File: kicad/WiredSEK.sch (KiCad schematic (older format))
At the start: 51 parts, among them J1 Conn_01x34, J2 USB_C_Receptacle, J3 AVR-JTAG-10, J4 Serial RX/TX, J5 Testpad, SW1 HWB_SW, SW2 RST_SW, U1 USBLC6-2SC6, U2 AT90USB646-AU, Y1 16 Mhz

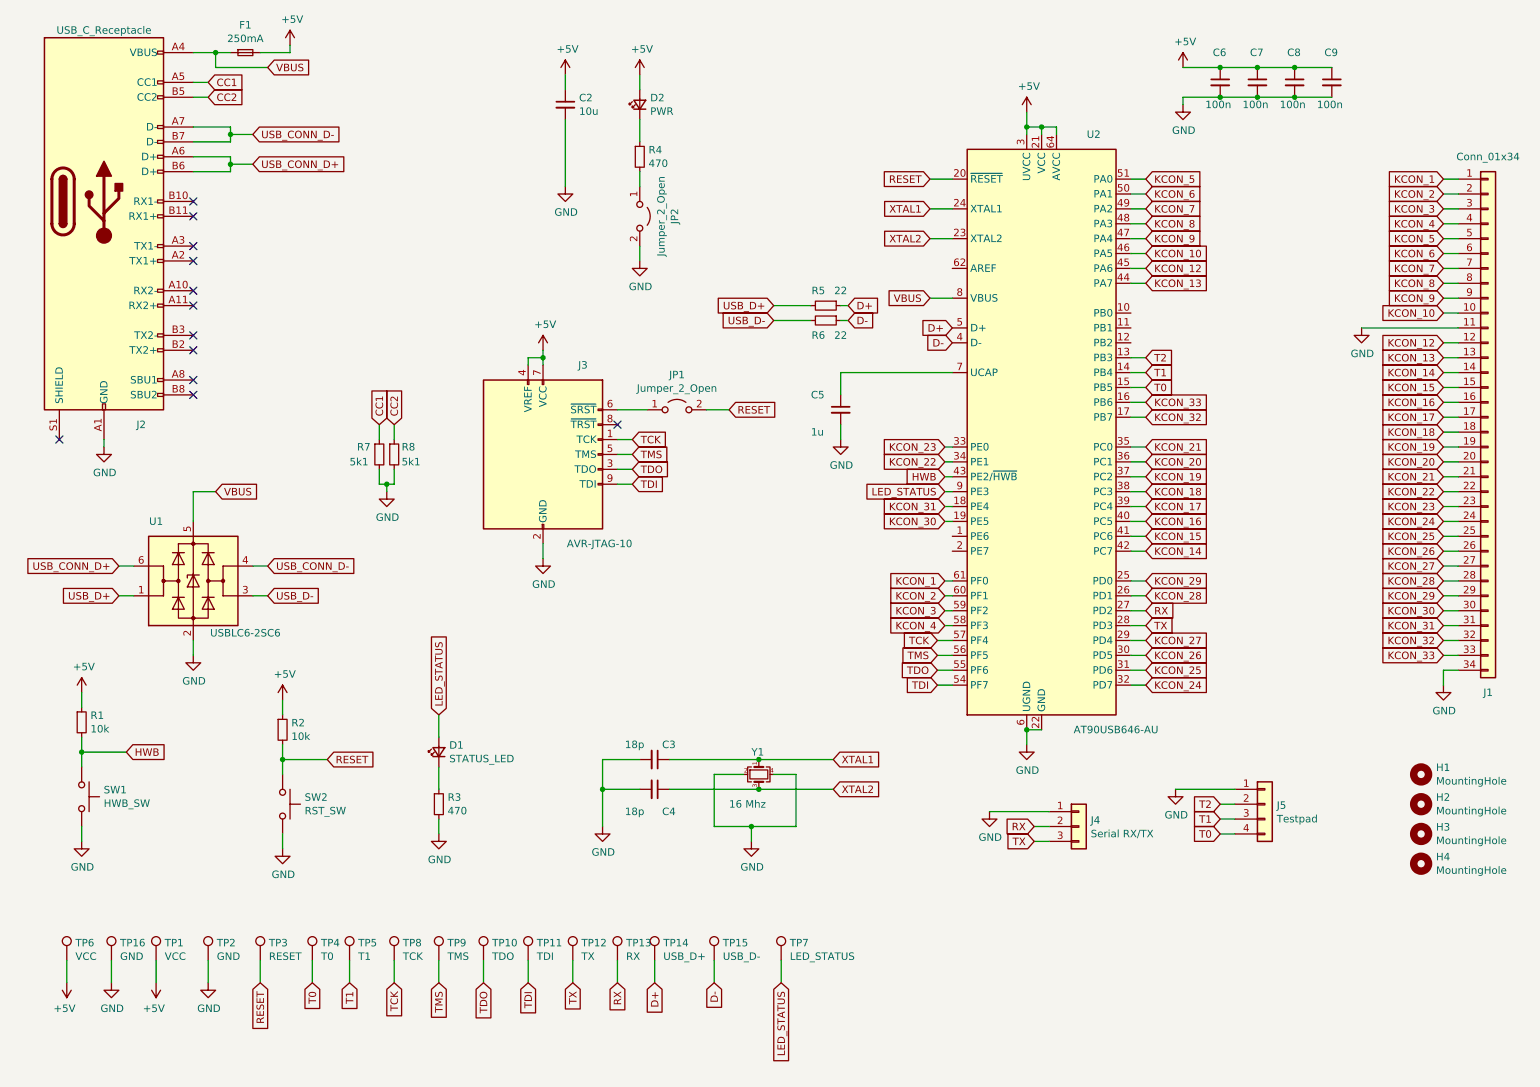
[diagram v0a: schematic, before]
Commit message: done with pcb routing
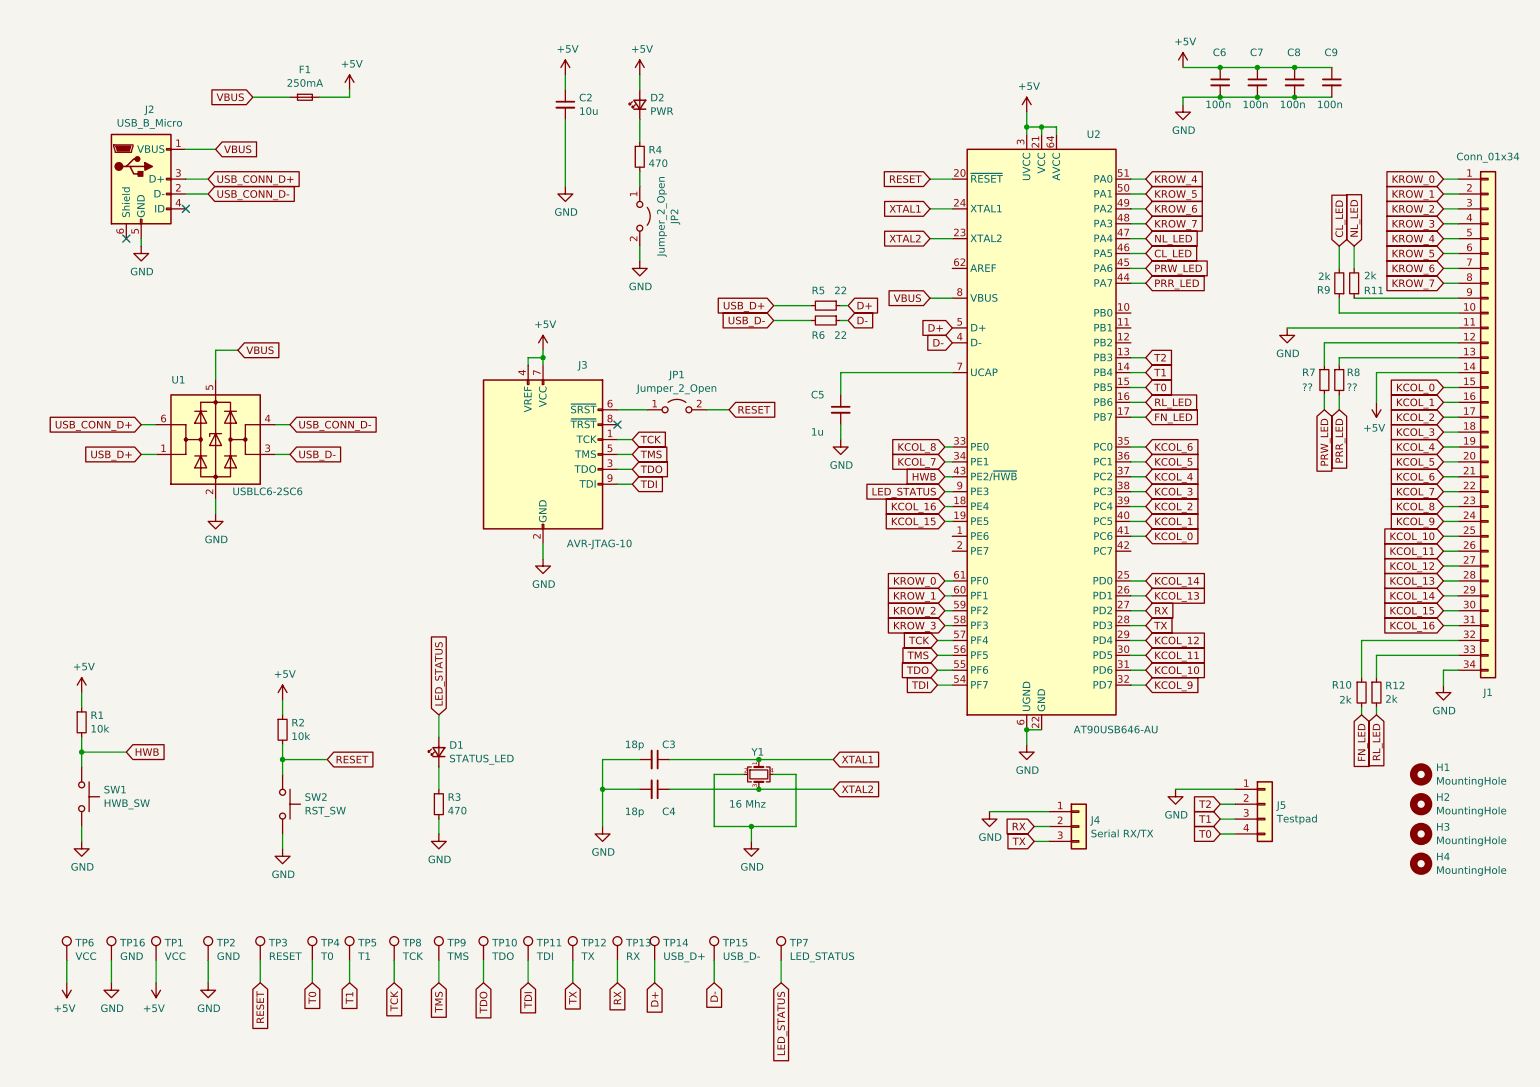
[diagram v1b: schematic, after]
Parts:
- removed J2: USB_C_Receptacle, WiredSEK:SJ121226, symbol Connector:USB_C_Receptacle
- added J2: USB_B_Micro, WiredSEK:GMCB05801124EU, symbol Connector:USB_B_Micro
- added R10, R11, R12, R9: 2k, Resistor_SMD:R_0805_2012Metric_Pad1.20x1.40mm_HandSolder, symbol Device:R_Small
- R7, R8: value 5k1 -> ??; JLCPCB C27834 -> C17710
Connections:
- net +5V: now also J1.14 (Pin_14)
- net GND: now also J2.5 (GND); no longer R7.2, R8.2
- net USB_CONN_D+: now also J2.3 (D+)
- net USB_CONN_D-: now also J2.2 (D-)
- net VBUS: now also J2.1 (VBUS)
- net CC1: no longer names the net of R7.1
- net CC1: now also J1.12 (Pin_12)
- net CC2: no longer names the net of R8.1
- net CC2: now also J1.13 (Pin_13)
- net KCON_1 renamed KROW_0
- net KCON_10: no longer names the net of J1.10 (Pin_10)
- net KCON_10: now also R9.1; no longer U2.46 (PA5)
- net KCON_12 renamed PRW_LED
- net PRW_LED: now also R7.2; no longer J1.12 (Pin_12)
- net KCON_13 renamed PRR_LED
- net PRR_LED: now also R8.2; no longer J1.13 (Pin_13)
- net KCON_14: no longer names the net of U2.42 (PC7)
- net KCON_14: no longer J1.14 (Pin_14)
- net KCON_15 renamed KCOL_0
- net KCON_16 renamed KCOL_1
- net KCON_17 renamed KCOL_2
- net KCON_18 renamed KCOL_3
- net KCON_19 renamed KCOL_4
- net KCON_2 renamed KROW_1
- net KCON_20 renamed KCOL_5
- net KCON_21 renamed KCOL_6
- net KCON_22 renamed KCOL_7
- net KCON_23 renamed KCOL_8
- net KCON_24 renamed KCOL_9
- net KCON_25 renamed KCOL_10
- net KCON_26 renamed KCOL_11
- net KCON_27 renamed KCOL_12
- net KCON_28 renamed KCOL_13
- net KCON_29 renamed KCOL_14
- net KCON_3 renamed KROW_2
- net KCON_30 renamed KCOL_15
- net KCON_31 renamed KCOL_16
- net KCON_32: no longer names the net of J1.32 (Pin_32)
- net KCON_32: now also R10.1; no longer U2.17 (PB7)
- net KCON_33: no longer names the net of J1.33 (Pin_33)
- net KCON_33: now also R12.1; no longer U2.16 (PB6)
- net KCON_4 renamed KROW_3
- net KCON_5 renamed KROW_4
- net KCON_6 renamed KROW_5
- net KCON_7 renamed KROW_6
- net KCON_8 renamed KROW_7
- net KCON_9: no longer names the net of J1.9 (Pin_9)
- net KCON_9: now also R11.1; no longer U2.47 (PA4)
- new net CL_LED: R9.2, U2.46 (PA5)
- new net FN_LED: R10.2, U2.17 (PB7)
- new net NL_LED: R11.2, U2.47 (PA4)
- new net RL_LED: R12.2, U2.16 (PB6)
- no-connect marks 12 -> 3
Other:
- moved on the sheet: F1, U1

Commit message: preparing for jlcpcb order
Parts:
- C2: JLCPCB C15850 -> (none); LCSC Part # (none) -> C15850
- C3, C4: JLCPCB C1647 -> (none); LCSC Part # (none) -> C1647
- C5: LCSC Part # (none) -> C15849
- C6, C7, C8, C9: JLCPCB C57112 -> (none); LCSC Part # (none) -> C57112
- D1: JLCPCB C72041 -> (none); LCSC Part # (none) -> C72041
- D2: JLCPCB C72043 -> (none); LCSC Part # (none) -> C72043
- F1: JLCPCB C369159 -> (none); LCSC Part # (none) -> C369159
- R1, R2: JLCPCB C17414 -> (none); LCSC Part # (none) -> C17414
- R10, R11, R12, R3, R4, R9: JLCPCB C17710 -> (none); LCSC Part # (none) -> C17710
- R5, R6: JLCPCB C25295 -> (none); LCSC Part # (none) -> C25295
- R7, R8: JLCPCB C17710 -> (none)
- SW1, SW2: JLCPCB C115357 -> (none); LCSC Part # (none) -> C115357
- U1: JLCPCB C558442 -> (none); LCSC Part # (none) -> C558442
- Y1: JLCPCB X1E000021011900 -> (none); LCSC Part # (none) -> X1E000021011900
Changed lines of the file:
@@
 F 2 "Package_TO_SOT_SMD:SOT-23-6" H 1900 2850 50  0001 C CNN
 F 3 "https://www.st.com/resource/en/datasheet/usblc6-2.pdf" H 2100 3700 50  0001 C CNN
-F 4 "C558442" H 1900 3350 50  0001 C CNN "JLCPCB"
+F 4 "C558442" H 1900 3350 50  0001 C CNN "LCSC Part #"
 	1    1900 3350
 	1    0    0    -1
@@
 F 2 "Resistor_SMD:R_0805_2012Metric_Pad1.20x1.40mm_HandSolder" H 6000 2450 50  0001 C CNN
 F 3 "~" H 6000 2450 50  0001 C CNN
-F 4 "C25295" V 6000 2450 50  0001 C CNN "JLCPCB"
+F 4 "C25295" H 6000 2450 50  0001 C CNN "LCSC Part #"
 	1    6000 2450
 	0    1    1    0
@@
 F 2 "Resistor_SMD:R_0805_2012Metric_Pad1.20x1.40mm_HandSolder" H 6000 2550 50  0001 C CNN
 F 3 "~" H 6000 2550 50  0001 C CNN
-F 4 "C25295" V 6000 2550 50  0001 C CNN "JLCPCB"
+F 4 "C25295" H 6000 2550 50  0001 C CNN "LCSC Part #"
 	1    6000 2550
 	0    1    1    0
@@
 F 2 "Capacitor_SMD:C_0603_1608Metric_Pad1.08x0.95mm_HandSolder" H 8650 950 50  0001 C CNN
 F 3 "~" H 8650 950 50  0001 C CNN
-F 4 "C57112" H 8650 950 50  0001 C CNN "JLCPCB"
+F 4 "C57112" H 8650 950 50  0001 C CNN "LCSC Part #"
 	1    8650 950
 	1    0    0    -1
@@
 F 2 "Capacitor_SMD:C_0603_1608Metric_Pad1.08x0.95mm_HandSolder" H 8900 950 50  0001 C CNN
 F 3 "~" H 8900 950 50  0001 C CNN
-F 4 "C57112" H 8900 950 50  0001 C CNN "JLCPCB"
+F 4 "C57112" H 8900 950 50  0001 C CNN "LCSC Part #"
 	1    8900 950
 	1    0    0    -1
@@
 F 2 "Capacitor_SMD:C_0603_1608Metric_Pad1.08x0.95mm_HandSolder" H 9150 950 50  0001 C CNN
 F 3 "~" H 9150 950 50  0001 C CNN
-F 4 "C57112" H 9150 950 50  0001 C CNN "JLCPCB"
+F 4 "C57112" H 9150 950 50  0001 C CNN "LCSC Part #"
 	1    9150 950
 	1    0    0    -1
@@
 F 2 "Capacitor_SMD:C_0603_1608Metric_Pad1.08x0.95mm_HandSolder" H 6100 3150 50  0001 C CNN
 F 3 "~" H 6100 3150 50  0001 C CNN
+F 4 "C15849" H 6100 3150 50  0001 C CNN "LCSC Part #"
 	1    6100 3150
 	1    0    0    -1
@@
 F 2 "Capacitor_SMD:C_0805_2012Metric_Pad1.18x1.45mm_HandSolder" H 4250 1100 50  0001 C CNN
 F 3 "~" H 4250 1100 50  0001 C CNN
-F 4 "C15850" H 4250 1100 50  0001 C CNN "JLCPCB"
+F 4 "C15850" H 4250 1100 50  0001 C CNN "LCSC Part #"
 	1    4250 1100
 	1    0    0    -1
@@
 	1    0    0    -1
 $EndComp
-Wire Wire Line
-	4250 1000 4250 900
 $Comp
 L Device:Crystal_GND24_Small Y1
@@
 F 2 "Crystal:Crystal_SMD_3225-4Pin_3.2x2.5mm_HandSoldering" H 5550 5600 50  0001 C CNN
 F 3 "~" H 5550 5600 50  0001 C CNN
-F 4 "X1E000021011900" V 5550 5600 50  0001 C CNN "JLCPCB"
+F 4 "X1E000021011900" H 5550 5600 50  0001 C CNN "LCSC Part #"
 	1    5550 5600
 	0    1    1    0
@@
 F 2 "Capacitor_SMD:C_0603_1608Metric_Pad1.08x0.95mm_HandSolder" H 4850 5500 50  0001 C CNN
 F 3 "~" H 4850 5500 50  0001 C CNN
-F 4 "C1647" V 4850 5500 50  0001 C CNN "JLCPCB"
+F 4 "C1647" H 4850 5500 50  0001 C CNN "LCSC Part #"
 	1    4850 5500
 	0    1    1    0
@@
 F 2 "Capacitor_SMD:C_0603_1608Metric_Pad1.08x0.95mm_HandSolder" H 4850 5700 50  0001 C CNN
 F 3 "~" H 4850 5700 50  0001 C CNN
-F 4 "C1647" V 4850 5700 50  0001 C CNN "JLCPCB"
+F 4 "C1647" H 4850 5700 50  0001 C CNN "LCSC Part #"
 	1    4850 5700
 	0    1    1    0
@@
 F 2 "Resistor_SMD:R_0805_2012Metric_Pad1.20x1.40mm_HandSolder" H 2350 5300 50  0001 C CNN
 F 3 "~" H 2350 5300 50  0001 C CNN
-F 4 "C17414" H 2350 5300 50  0001 C CNN "JLCPCB"
+F 4 "C17414" H 2350 5300 50  0001 C CNN "LCSC Part #"
 	1    2350 5300
 	1    0    0    -1
@@
 F 2 "WiredSEK:SKRKAEE020" H 2350 6000 50  0001 C CNN
 F 3 "~" H 2350 6000 50  0001 C CNN
-F 4 "C115357" V 2350 5800 50  0001 C CNN "JLCPCB"
+F 4 "C115357" H 2350 5800 50  0001 C CNN "LCSC Part #"
 	1    2350 5800
 	0    1    1    0
@@
 F 2 "Fuse:Fuse_1206_3216Metric_Pad1.42x1.75mm_HandSolder" H 2500 1050 50  0001 C CNN
 F 3 "~" H 2500 1050 50  0001 C CNN
-F 4 "C369159" H 2500 1050 50  0001 C CNN "JLCPCB"
+F 4 "C369159" H 2500 1050 50  0001 C CNN "LCSC Part #"
 	1    2500 1050
 	1    0    0    -1
@@
 F 2 "Resistor_SMD:R_0805_2012Metric_Pad1.20x1.40mm_HandSolder" H 1000 5250 50  0001 C CNN
 F 3 "~" H 1000 5250 50  0001 C CNN
-F 4 "C17414" H 1000 5250 50  0001 C CNN "JLCPCB"
+F 4 "C17414" H 1000 5250 50  0001 C CNN "LCSC Part #"
 	1    1000 5250
 	1    0    0    -1
@@
 F 2 "WiredSEK:SKRKAEE020" H 1000 5950 50  0001 C CNN
 F 3 "~" H 1000 5950 50  0001 C CNN
-F 4 "C115357" V 1000 5750 50  0001 C CNN "JLCPCB"
+F 4 "C115357" H 1000 5750 50  0001 C CNN "LCSC Part #"
 	1    1000 5750
 	0    1    1    0
@@
 F 2 "LED_SMD:LED_0603_1608Metric_Pad1.05x0.95mm_HandSolder" V 3400 5450 50  0001 C CNN
 F 3 "~" V 3400 5450 50  0001 C CNN
-F 4 "C72041" V 3400 5450 50  0001 C CNN "JLCPCB"
+F 4 "C72041" H 3400 5450 50  0001 C CNN "LCSC Part #"
 	1    3400 5450
 	0    -1   -1   0
@@
 F 2 "Resistor_SMD:R_0805_2012Metric_Pad1.20x1.40mm_HandSolder" H 3400 5800 50  0001 C CNN
 F 3 "~" H 3400 5800 50  0001 C CNN
-F 4 "C17710" H 3400 5800 50  0001 C CNN "JLCPCB"
+F 4 "C17710" H 3400 5800 50  0001 C CNN "LCSC Part #"
 	1    3400 5800
 	1    0    0    -1
@@
 F 2 "LED_SMD:LED_0603_1608Metric_Pad1.05x0.95mm_HandSolder" V 4750 1100 50  0001 C CNN
 F 3 "~" V 4750 1100 50  0001 C CNN
-F 4 "C72043" V 4750 1100 50  0001 C CNN "JLCPCB"
+F 4 "C72043" H 4750 1100 50  0001 C CNN "LCSC Part #"
 	1    4750 1100
 	0    -1   -1   0
@@
 F 2 "Resistor_SMD:R_0805_2012Metric_Pad1.20x1.40mm_HandSolder" H 4750 1450 50  0001 C CNN
 F 3 "~" H 4750 1450 50  0001 C CNN
-F 4 "C17710" H 4750 1450 50  0001 C CNN "JLCPCB"
+F 4 "C17710" H 4750 1450 50  0001 C CNN "LCSC Part #"
 	1    4750 1450
 	1    0    0    -1
@@
 F 2 "Capacitor_SMD:C_0603_1608Metric_Pad1.08x0.95mm_HandSolder" H 9400 950 50  0001 C CNN
 F 3 "~" H 9400 950 50  0001 C CNN
-F 4 "C57112" H 9400 950 50  0001 C CNN "JLCPCB"
+F 4 "C57112" H 9400 950 50  0001 C CNN "LCSC Part #"
 	1    9400 950
 	1    0    0    -1
@@
 F 2 "Resistor_SMD:R_0805_2012Metric_Pad1.20x1.40mm_HandSolder" H 9700 5050 50  0001 C CNN
 F 3 "~" H 9700 5050 50  0001 C CNN
-F 4 "C17710" H 9700 5050 50  0001 C CNN "JLCPCB"
+F 4 "C17710" H 9700 5050 50  0001 C CNN "LCSC Part #"
 	1    9700 5050
 	1    0    0    -1
@@
 F 2 "Resistor_SMD:R_0805_2012Metric_Pad1.20x1.40mm_HandSolder" H 9600 5050 50  0001 C CNN
 F 3 "~" H 9600 5050 50  0001 C CNN
-F 4 "C17710" H 9600 5050 50  0001 C CNN "JLCPCB"
+F 4 "C17710" H 9600 5050 50  0001 C CNN "LCSC Part #"
 	1    9600 5050
 	1    0    0    -1
@@
 F 2 "Resistor_SMD:R_0805_2012Metric_Pad1.20x1.40mm_HandSolder" H 9450 2300 50  0001 C CNN
 F 3 "~" H 9450 2300 50  0001 C CNN
-F 4 "C17710" H 9450 2300 50  0001 C CNN "JLCPCB"
+F 4 "C17710" H 9450 2300 50  0001 C CNN "LCSC Part #"
 	1    9450 2300
 	-1   0    0    1
@@
 F 2 "Resistor_SMD:R_0805_2012Metric_Pad1.20x1.40mm_HandSolder" H 9550 2300 50  0001 C CNN
 F 3 "~" H 9550 2300 50  0001 C CNN
-F 4 "C17710" H 9550 2300 50  0001 C CNN "JLCPCB"
+F 4 "C17710" H 9550 2300 50  0001 C CNN "LCSC Part #"
 	1    9550 2300
 	-1   0    0    1
@@
 F 2 "Resistor_SMD:R_0805_2012Metric_Pad1.20x1.40mm_HandSolder" H 9350 2950 50  0001 C CNN
 F 3 "~" H 9350 2950 50  0001 C CNN
-F 4 "C17710" H 9350 2950 50  0001 C CNN "JLCPCB"
+F 4 "" H 9350 2950 50  0001 C CNN "LCSC Part #"
 	1    9350 2950
 	1    0    0    -1
@@
 F 2 "Resistor_SMD:R_0805_2012Metric_Pad1.20x1.40mm_HandSolder" H 9450 2950 50  0001 C CNN
 F 3 "~" H 9450 2950 50  0001 C CNN
-F 4 "C17710" H 9450 2950 50  0001 C CNN "JLCPCB"
+F 4 "" H 9450 2950 50  0001 C CNN "LCSC Part #"
 	1    9450 2950
 	1    0    0    -1
@@
 	2150 1050 2400 1050
 NoConn ~ 1700 1800
+Wire Wire Line
+	4250 900  4250 1000
 $EndSCHEMATC
